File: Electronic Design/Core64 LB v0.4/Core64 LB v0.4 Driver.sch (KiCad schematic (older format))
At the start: 65 parts, among them J1 SSW-116-22-F-S-VS‎, J5 SSW-116-22-F-S-VS‎, Q1 MMBT4403LT1G, Q10 MMBT4403LT1G, Q11 MMBT4403LT1G, Q12 MMBT4401LT1G, Q13 MMBT4403LT1G, Q14 MMBT4403LT1G, Q15 MMBT4401LT1G, Q16 MMBT4403LT1G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

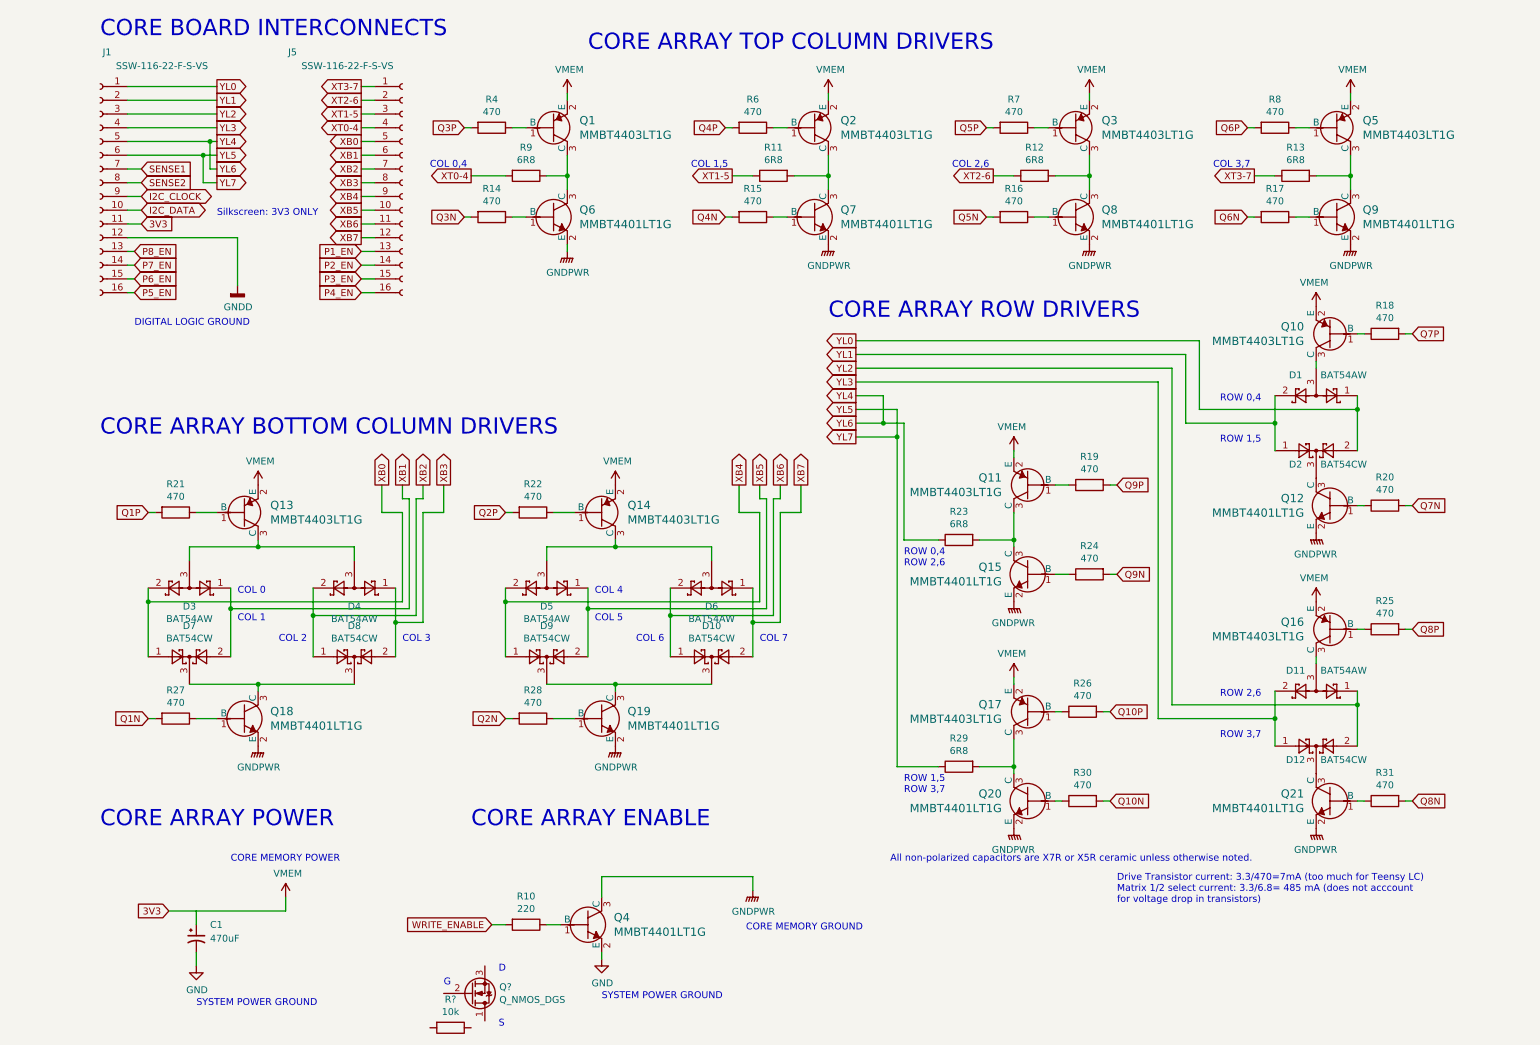
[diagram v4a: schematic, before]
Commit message: Update schematic and XLS pin usage
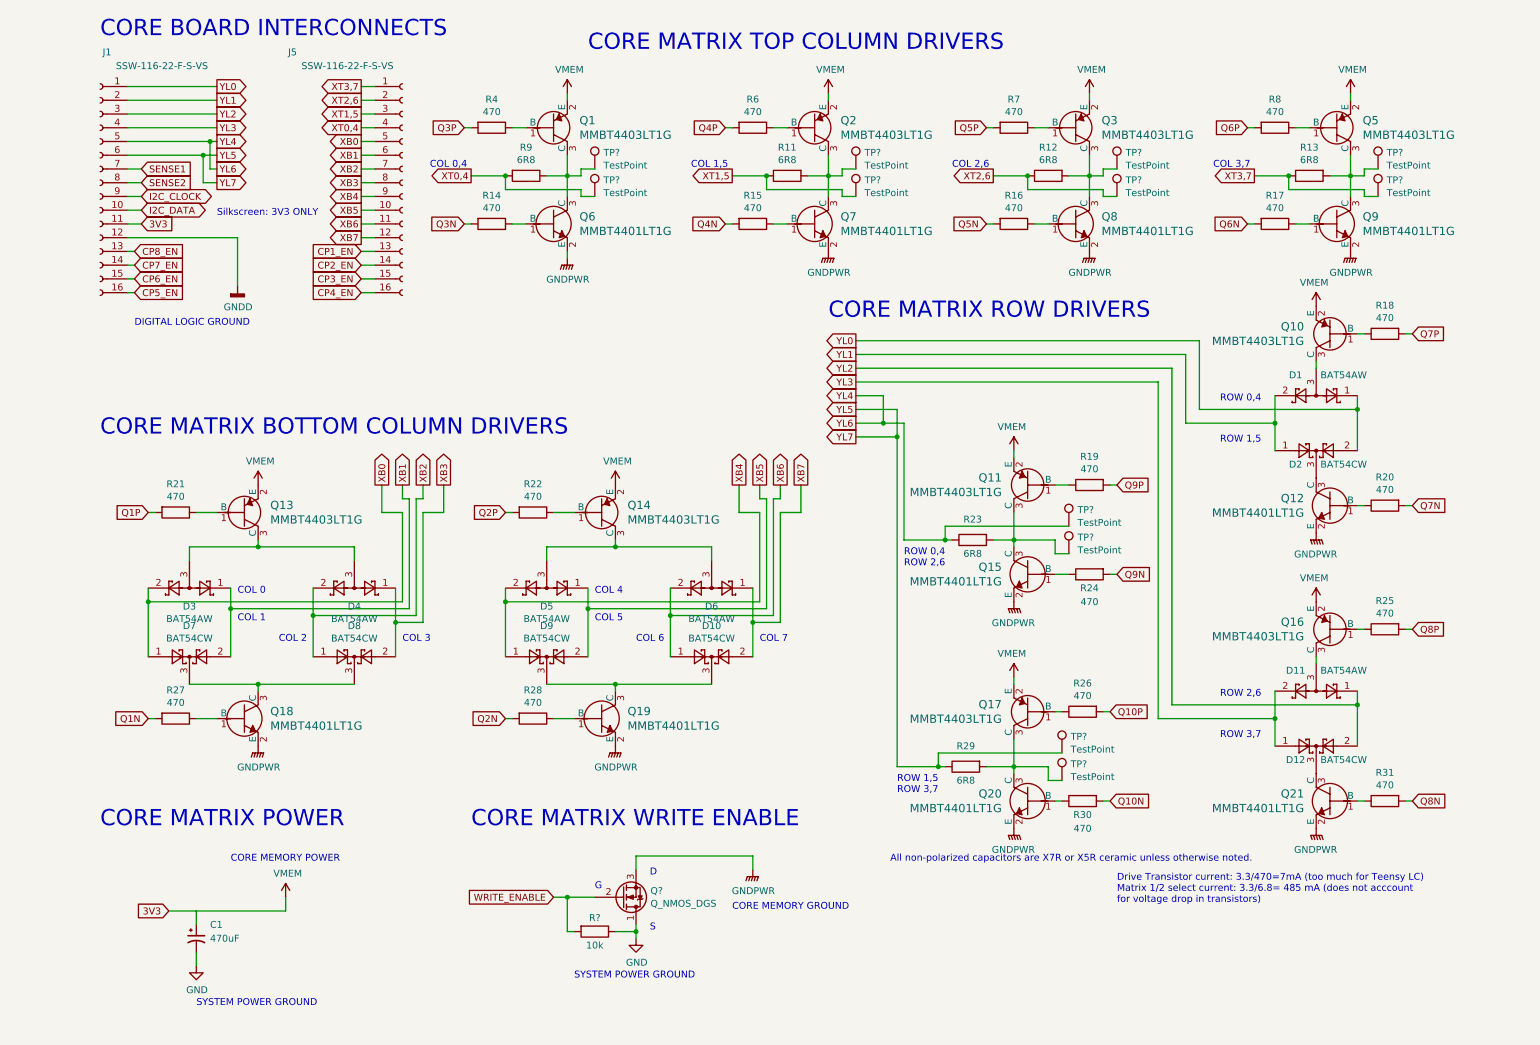
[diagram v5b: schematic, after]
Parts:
- removed Q4: MMBT4401LT1G, Digikey:SOT-23-3, symbol Digikey-Transistors:MMBT4401LT1G
- removed R10: 220, Resistor_SMD:R_0805_2012Metric, symbol Device:R
- added TP? (x12): TestPoint, TestPoint:TestPoint_THTPad_2.5x2.5mm_Drill1.2mm, symbol Connector:TestPoint
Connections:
- net GND: now also Q?.1 (D), R?.1
- net GNDPWR: now also Q?.3 (S)
- net WRITE_ENABLE: now also Q?.2 (G), R?.2
- net YL4: now also TP?.1
- net YL5: now also TP?.1
- net at Q1.3 (C), Q6.3 (C), R9.1: now also TP?.1
- net at Q2.3 (C), Q7.3 (C), R11.2: now also TP?.1
- net at Q3.3 (C), Q8.3 (C), R12.2: now also TP?.1
- net at Q5.3 (C), Q9.3 (C), R13.2: now also TP?.1
- net at Q11.3 (C), Q15.3 (C), R23.2: now also TP?.1
- net at Q17.3 (C), Q20.3 (C), R29.2: now also TP?.1
- net P1_EN renamed CP1_EN
- net P2_EN renamed CP2_EN
- net P3_EN renamed CP3_EN
- net P4_EN renamed CP4_EN
- net P5_EN renamed CP5_EN
- net P6_EN renamed CP6_EN
- net P7_EN renamed CP7_EN
- net P8_EN renamed CP8_EN
- net XT0-4 renamed XT0,4
- net XT0,4: now also TP?.1
- net XT1-5 renamed XT1,5
- net XT1,5: now also TP?.1
- net XT2-6 renamed XT2,6
- net XT2,6: now also TP?.1
- net XT3-7 renamed XT3,7
- net XT3,7: now also TP?.1
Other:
- note added: "CORE MATRIX BOTTOM COLUMN DRIVERS"
- note added: "CORE MATRIX POWER"
- note added: "CORE MATRIX ROW DRIVERS"
- note added: "CORE MATRIX TOP COLUMN DRIVERS"
- note added: "CORE MATRIX WRITE ENABLE"
- note removed: "CORE ARRAY BOTTOM COLUMN DRIVERS"
- note removed: "CORE ARRAY ENABLE"
- note removed: "CORE ARRAY POWER"
- note removed: "CORE ARRAY ROW DRIVERS"
- note removed: "CORE ARRAY TOP COLUMN DRIVERS"
- moved on the sheet: Q6, Q7, Q8, Q9, Q?, R11, R12, R13, R14, R15, R16, R17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

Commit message: Update schematic
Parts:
- added J13: Core Cur. Mon., Connector_PinSocket_2.54mm:PinSocket_1x02_P2.54mm_Vertical, symbol Connector_Generic:Conn_01x02
- J1, J5: symbol Connector:Conn_01x16_Female -> Connector_Generic:Conn_01x16
- Q4: renamed from Q?; value Q_NMOS_DGS -> Q_PMOS_DGS_BSS315PH6327XTSA1; footprint (none) -> Digikey:SOT-23-3; symbol Device:Q_NMOS_DGS -> Device:Q_PMOS_DGS
- TP1, TP10, TP11, TP12, TP2, TP3, TP4, TP5, TP6, TP7, TP8, TP9: renamed from TP?; footprint TestPoint:TestPoint_THTPad_2.5x2.5mm_Drill1.2mm -> Connector_PinSocket_2.54mm:PinSocket_1x01_P2.54mm_Vertical
- gave numbers to parts that had none: 1
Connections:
- net VMEM: now also C1.1, J13.1 (Pin_1), J13.2 (Pin_2)
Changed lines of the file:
@@
 Text GLabel 3850 7000 0    50   Input ~ 0
 WRITE_ENABLE
-Text Notes 5150 7100 0    50   ~ 0
+Text Notes 4900 6700 0    50   ~ 0
 CORE MEMORY GROUND
 Wire Wire Line
@@
 L power:GNDPWR #PWR?
 U 1 1 5E8ED56D
-P 5300 6800
+P 5300 6750
 AR Path="/5E8ED56D" Ref="#PWR?"  Part="1"
 AR Path="/5D254AE8/5E8ED56D" Ref="#PWR?"  Part="1"
 AR Path="/5E755AC8/5E8ED56D" Ref="#PWR0151"  Part="1"
-F 0 "#PWR0151" H 5300 6600 50  0001 C CNN
-F 1 "GNDPWR" H 5304 6646 50  0000 C CNN
-F 2 "" H 5300 6750 50  0001 C CNN
-F 3 "" H 5300 6750 50  0001 C CNN
-	1    5300 6800
+F 0 "#PWR0151" H 5300 6550 50  0001 C CNN
+F 1 "GNDPWR" H 5304 6596 50  0000 C CNN
+F 2 "" H 5300 6700 50  0001 C CNN
+F 3 "" H 5300 6700 50  0001 C CNN
+	1    5300 6750
 	1    0    0    -1
 $EndComp
 Wire Wire Line
 	3850 7000 3950 7000
-Text Notes 1500 6750 0    50   ~ 0
+Text Notes 2000 6750 0    50   ~ 0
 CORE MEMORY POWER
 Text GLabel 1050 7100 0    50   Input ~ 0
@@
 	5350 4200 5200 4200
 Wire Wire Line
-	5300 6700 5300 6800
+	5300 6700 5300 6750
 Connection ~ 6350 3650
 Wire Wire Line
@@
 L power:VMEM #PWR0143
 U 1 1 5EC965BD
-P 1900 7000
-F 0 "#PWR0143" H 1900 6850 50  0001 C CNN
-F 1 "VMEM" H 1915 7173 50  0000 C CNN
-F 2 "" H 1900 7000 50  0001 C CNN
-F 3 "" H 1900 7000 50  0001 C CNN
-	1    1900 7000
-	1    0    0    -1
-$EndComp
-Wire Wire Line
-	1900 7100 1900 7000
+P 2200 7000
+F 0 "#PWR0143" H 2200 6850 50  0001 C CNN
+F 1 "VMEM" H 2215 7173 50  0000 C CNN
+F 2 "" H 2200 7000 50  0001 C CNN
+F 3 "" H 2200 7000 50  0001 C CNN
+	1    2200 7000
+	1    0    0    -1
+$EndComp
+Wire Wire Line
+	2200 7100 2200 7000
 Text Notes 3250 6500 0    118  ~ 0
 CORE MATRIX WRITE ENABLE
@@
 	2450 2100 2550 2100
 $Comp
-L Connector:Conn_01x16_Female J5
+L Connector_Generic:Conn_01x16 J5
 U 1 1 5E78B5ED
 P 2750 1800
@@
 $EndComp
 $Comp
-L Connector:Conn_01x16_Female J1
+L Connector_Generic:Conn_01x16 J1
 U 1 1 5E78B5F3
 P 550 1800
@@
 	3950 2300 3950 2350
 Wire Wire Line
-	1050 7100 1900 7100
-Wire Wire Line
-	1250 7100 1250 7200
+	1050 7100 1250 7100
 $Comp
 L power:GND #PWR?
@@
 	2550 2600 2450 2600
 $Comp
-L Device:Q_NMOS_DGS Q?
+L Device:Q_PMOS_DGS Q4
 U 1 1 5F6BF8B4
 P 4350 7000
-F 0 "Q?" H 4555 6953 50  0000 L CNN
-F 1 "Q_NMOS_DGS" H 4555 7046 50  0000 L CNN
-F 2 "" H 4550 7100 50  0001 C CNN
+F 0 "Q4" H 4555 6953 50  0000 L CNN
+F 1 "Q_PMOS_DGS_BSS315PH6327XTSA1" H 4555 7046 50  0000 L CNN
+F 2 "Digikey:SOT-23-3" H 4550 7100 50  0001 C CNN
 F 3 "~" H 4350 7000 50  0001 C CNN
 	1    4350 7000
@@
 AR Path="/5F6E9DAB" Ref="R?"  Part="1"
 AR Path="/5D254AE8/5F6E9DAB" Ref="R?"  Part="1"
-AR Path="/5E755AC8/5F6E9DAB" Ref="R?"  Part="1"
-F 0 "R?" V 4050 7250 50  0000 C CNN
+AR Path="/5E755AC8/5F6E9DAB" Ref="R49"  Part="1"
+F 0 "R49" V 4050 7250 50  0000 C CNN
 F 1 "10k" V 4250 7250 50  0000 C CNN
 F 2 "Resistor_SMD:R_0805_2012Metric" V 4080 7250 50  0001 C CNN
@@
 $EndComp
 $Comp
-L Connector:TestPoint TP?
+L Connector:TestPoint TP1
 U 1 1 5FCDFD13
 P 4150 1700
-F 0 "TP?" H 4213 1819 50  0000 L CNN
+F 0 "TP1" H 4213 1819 50  0000 L CNN
 F 1 "TestPoint" H 4213 1726 50  0000 L CNN
-F 2 "TestPoint:TestPoint_THTPad_2.5x2.5mm_Drill1.2mm" H 4350 1700 50  0001 C CNN
+F 2 "Connector_PinSocket_2.54mm:PinSocket_1x01_P2.54mm_Vertical" H 4350 1700 50  0001 C CNN
 F 3 "~" H 4350 1700 50  0001 C CNN
 	1    4150 1700
@@
 $EndComp
 $Comp
-L Connector:TestPoint TP?
+L Connector:TestPoint TP5
 U 1 1 5FCE3594
 P 4150 1900
-F 0 "TP?" H 4213 2019 50  0000 L CNN
+F 0 "TP5" H 4213 2019 50  0000 L CNN
 F 1 "TestPoint" H 4213 1926 50  0000 L CNN
-F 2 "TestPoint:TestPoint_THTPad_2.5x2.5mm_Drill1.2mm" H 4350 1900 50  0001 C CNN
+F 2 "Connector_PinSocket_2.54mm:PinSocket_1x01_P2.54mm_Vertical" H 4350 1900 50  0001 C CNN
 F 3 "~" H 4350 1900 50  0001 C CNN
 	1    4150 1900
@@
 	3500 1850 4050 1850
 $Comp
-L Connector:TestPoint TP?
+L Connector:TestPoint TP2
 U 1 1 5FDC2F4B
 P 6050 1700
-F 0 "TP?" H 6113 1819 50  0000 L CNN
+F 0 "TP2" H 6113 1819 50  0000 L CNN
 F 1 "TestPoint" H 6113 1726 50  0000 L CNN
-F 2 "TestPoint:TestPoint_THTPad_2.5x2.5mm_Drill1.2mm" H 6250 1700 50  0001 C CNN
+F 2 "Connector_PinSocket_2.54mm:PinSocket_1x01_P2.54mm_Vertical" H 6250 1700 50  0001 C CNN
 F 3 "~" H 6250 1700 50  0001 C CNN
 	1    6050 1700
@@
 $EndComp
 $Comp
-L Connector:TestPoint TP?
+L Connector:TestPoint TP6
 U 1 1 5FDC2F51
 P 6050 1900
-F 0 "TP?" H 6113 2019 50  0000 L CNN
+F 0 "TP6" H 6113 2019 50  0000 L CNN
 F 1 "TestPoint" H 6113 1926 50  0000 L CNN
-F 2 "TestPoint:TestPoint_THTPad_2.5x2.5mm_Drill1.2mm" H 6250 1900 50  0001 C CNN
+F 2 "Connector_PinSocket_2.54mm:PinSocket_1x01_P2.54mm_Vertical" H 6250 1900 50  0001 C CNN
 F 3 "~" H 6250 1900 50  0001 C CNN
 	1    6050 1900
@@
 	5400 1850 5950 1850
 $Comp
-L Connector:TestPoint TP?
+L Connector:TestPoint TP3
 U 1 1 5FDD3A8B
 P 7950 1700
-F 0 "TP?" H 8013 1819 50  0000 L CNN
+F 0 "TP3" H 8013 1819 50  0000 L CNN
 F 1 "TestPoint" H 8013 1726 50  0000 L CNN
-F 2 "TestPoint:TestPoint_THTPad_2.5x2.5mm_Drill1.2mm" H 8150 1700 50  0001 C CNN
+F 2 "Connector_PinSocket_2.54mm:PinSocket_1x01_P2.54mm_Vertical" H 8150 1700 50  0001 C CNN
 F 3 "~" H 8150 1700 50  0001 C CNN
 	1    7950 1700
@@
 $EndComp
 $Comp
-L Connector:TestPoint TP?
+L Connector:TestPoint TP7
 U 1 1 5FDD3A91
 P 7950 1900
-F 0 "TP?" H 8013 2019 50  0000 L CNN
+F 0 "TP7" H 8013 2019 50  0000 L CNN
 F 1 "TestPoint" H 8013 1926 50  0000 L CNN
-F 2 "TestPoint:TestPoint_THTPad_2.5x2.5mm_Drill1.2mm" H 8150 1900 50  0001 C CNN
+F 2 "Connector_PinSocket_2.54mm:PinSocket_1x01_P2.54mm_Vertical" H 8150 1900 50  0001 C CNN
 F 3 "~" H 8150 1900 50  0001 C CNN
 	1    7950 1900
@@
 	7300 1850 7850 1850
 $Comp
-L Connector:TestPoint TP?
+L Connector:TestPoint TP4
 U 1 1 5FDE4C7A
 P 9850 1700
-F 0 "TP?" H 9913 1819 50  0000 L CNN
+F 0 "TP4" H 9913 1819 50  0000 L CNN
 F 1 "TestPoint" H 9913 1726 50  0000 L CNN
-F 2 "TestPoint:TestPoint_THTPad_2.5x2.5mm_Drill1.2mm" H 10050 1700 50  0001 C CNN
+F 2 "Connector_PinSocket_2.54mm:PinSocket_1x01_P2.54mm_Vertical" H 10050 1700 50  0001 C CNN
 F 3 "~" H 10050 1700 50  0001 C CNN
 	1    9850 1700
@@
 $EndComp
 $Comp
-L Connector:TestPoint TP?
+L Connector:TestPoint TP8
 U 1 1 5FDE4C80
 P 9850 1900
-F 0 "TP?" H 9913 2019 50  0000 L CNN
+F 0 "TP8" H 9913 2019 50  0000 L CNN
 F 1 "TestPoint" H 9913 1926 50  0000 L CNN
-F 2 "TestPoint:TestPoint_THTPad_2.5x2.5mm_Drill1.2mm" H 10050 1900 50  0001 C CNN
+F 2 "Connector_PinSocket_2.54mm:PinSocket_1x01_P2.54mm_Vertical" H 10050 1900 50  0001 C CNN
 F 3 "~" H 10050 1900 50  0001 C CNN
 	1    9850 1900
@@
 Connection ~ 9200 1750
 $Comp
-L Connector:TestPoint TP?
+L Connector:TestPoint TP9
 U 1 1 5FE66091
 P 7600 4300
-F 0 "TP?" H 7663 4419 50  0000 L CNN
+F 0 "TP9" H 7663 4419 50  0000 L CNN
 F 1 "TestPoint" H 7663 4326 50  0000 L CNN
-F 2 "TestPoint:TestPoint_THTPad_2.5x2.5mm_Drill1.2mm" H 7800 4300 50  0001 C CNN
+F 2 "Connector_PinSocket_2.54mm:PinSocket_1x01_P2.54mm_Vertical" H 7800 4300 50  0001 C CNN
 F 3 "~" H 7800 4300 50  0001 C CNN
 	1    7600 4300
@@
 $EndComp
 $Comp
-L Connector:TestPoint TP?
+L Connector:TestPoint TP10
 U 1 1 5FE66097
 P 7600 4500
-F 0 "TP?" H 7663 4619 50  0000 L CNN
+F 0 "TP10" H 7663 4619 50  0000 L CNN
 F 1 "TestPoint" H 7663 4526 50  0000 L CNN
-F 2 "TestPoint:TestPoint_THTPad_2.5x2.5mm_Drill1.2mm" H 7800 4500 50  0001 C CNN
+F 2 "Connector_PinSocket_2.54mm:PinSocket_1x01_P2.54mm_Vertical" H 7800 4500 50  0001 C CNN
 F 3 "~" H 7800 4500 50  0001 C CNN
 	1    7600 4500
@@
 	6700 4300 7600 4300
 $Comp
-L Connector:TestPoint TP?
+L Connector:TestPoint TP11
 U 1 1 5FEFA1E9
 P 7550 5950
-F 0 "TP?" H 7613 6069 50  0000 L CNN
+F 0 "TP11" H 7613 6069 50  0000 L CNN
 F 1 "TestPoint" H 7613 5976 50  0000 L CNN
-F 2 "TestPoint:TestPoint_THTPad_2.5x2.5mm_Drill1.2mm" H 7750 5950 50  0001 C CNN
+F 2 "Connector_PinSocket_2.54mm:PinSocket_1x01_P2.54mm_Vertical" H 7750 5950 50  0001 C CNN
 F 3 "~" H 7750 5950 50  0001 C CNN
 	1    7550 5950
@@
 $EndComp
 $Comp
-L Connector:TestPoint TP?
+L Connector:TestPoint TP12
 U 1 1 5FEFA1EF
 P 7550 6150
-F 0 "TP?" H 7613 6269 50  0000 L CNN
+F 0 "TP12" H 7613 6269 50  0000 L CNN
 F 1 "TestPoint" H 7613 6176 50  0000 L CNN
-F 2 "TestPoint:TestPoint_THTPad_2.5x2.5mm_Drill1.2mm" H 7750 6150 50  0001 C CNN
+F 2 "Connector_PinSocket_2.54mm:PinSocket_1x01_P2.54mm_Vertical" H 7750 6150 50  0001 C CNN
 F 3 "~" H 7750 6150 50  0001 C CNN
 	1    7550 6150
@@
 Wire Wire Line
 	6650 6050 6700 6050
+Wire Wire Line
+	1250 7200 1250 7100
+Connection ~ 1250 7100
+Wire Wire Line
+	1250 7100 1600 7100
+$Comp
+L Connector_Generic:Conn_01x02 J?
+U 1 1 5F97E8E3
+P 1600 6900
+AR Path="/5E7548ED/5F97E8E3" Ref="J?"  Part="1"
+AR Path="/5E755AC8/5F97E8E3" Ref="J13"  Part="1"
+F 0 "J13" V 1700 6900 50  0000 R CNN
+F 1 "Core Cur. Mon." V 1800 7200 50  0000 R CNN
+F 2 "Connector_PinSocket_2.54mm:PinSocket_1x02_P2.54mm_Vertical" H 1600 6900 50  0001 C CNN
+F 3 "~" H 1600 6900 50  0001 C CNN
+	1    1600 6900
+	0    -1   -1   0
+$EndComp
+Wire Wire Line
+	1600 7100 1700 7100
+Wire Wire Line
+	1700 7100 2200 7100
+Connection ~ 1600 7100
+Connection ~ 1700 7100
 $EndSCHEMATC

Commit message: Update footprint mounting holes TFT, LED array, battery packs, lipo charger, arrange components to fit on the board
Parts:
- C1: footprint Capacitor_SMD:CP_Elec_10x10 -> Capacitor_SMD:CP_Elec_6.3x7.7
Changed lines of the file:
@@
 F 0 "C1" H 1350 7400 50  0000 L CNN
 F 1 "470uF" H 1350 7300 50  0000 L CNN
-F 2 "Capacitor_SMD:CP_Elec_10x10" H 1250 7300 50  0001 C CNN
+F 2 "Capacitor_SMD:CP_Elec_6.3x7.7" H 1250 7300 50  0001 C CNN
 F 3 "~" H 1250 7300 50  0001 C CNN
 F 4 "565-EMHL100ARA471MHA0GCT-ND" H 1250 7300 50  0001 C CNN "Digikey"

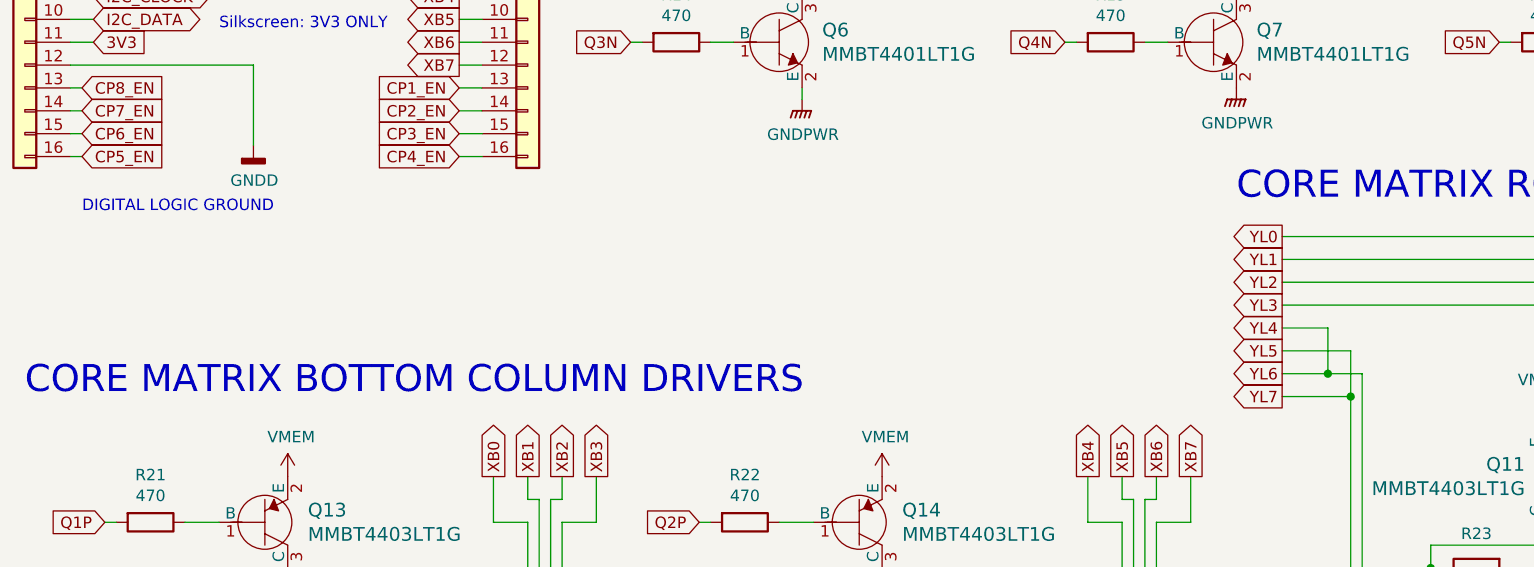
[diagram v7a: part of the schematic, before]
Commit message: Review and tweak Logic Board (LB) schematic, pin usage
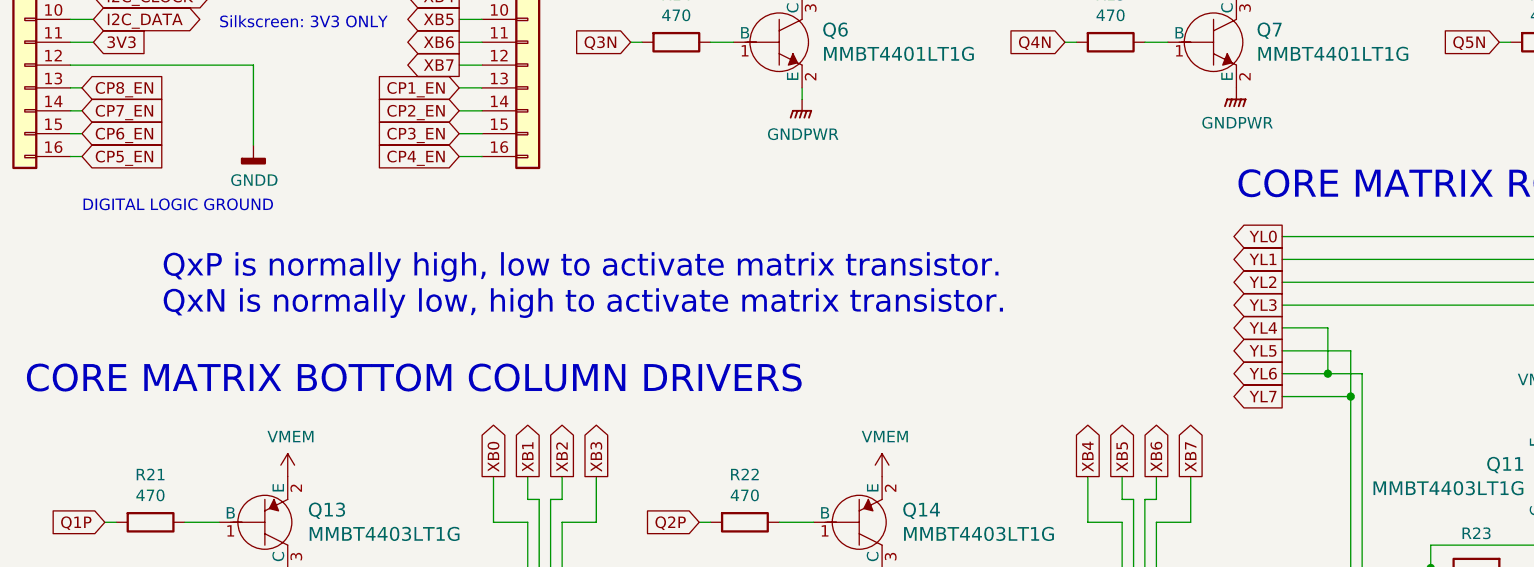
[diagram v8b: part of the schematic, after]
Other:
- note added: "QxP is normally high, low to activate matrix transistor.\nQxN is normally low, high to activate matrix transistor."
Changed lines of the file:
@@
 Connection ~ 1600 7100
 Connection ~ 1700 7100
+Text Notes 1150 3300 0    98   ~ 0
+QxP is normally high, low to activate matrix transistor.\nQxN is normally low, high to activate matrix transistor.
 $EndSCHEMATC
